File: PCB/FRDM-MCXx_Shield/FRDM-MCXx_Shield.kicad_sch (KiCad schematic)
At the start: 16 parts, among them J2 Conn_01x03_Pin, J3 Conn_01x02_Pin, J4 Conn_01x04_Pin, J5 Barrel_Jack_Switch, Q1 IRLML6401, U1 M95010-RMN6TP

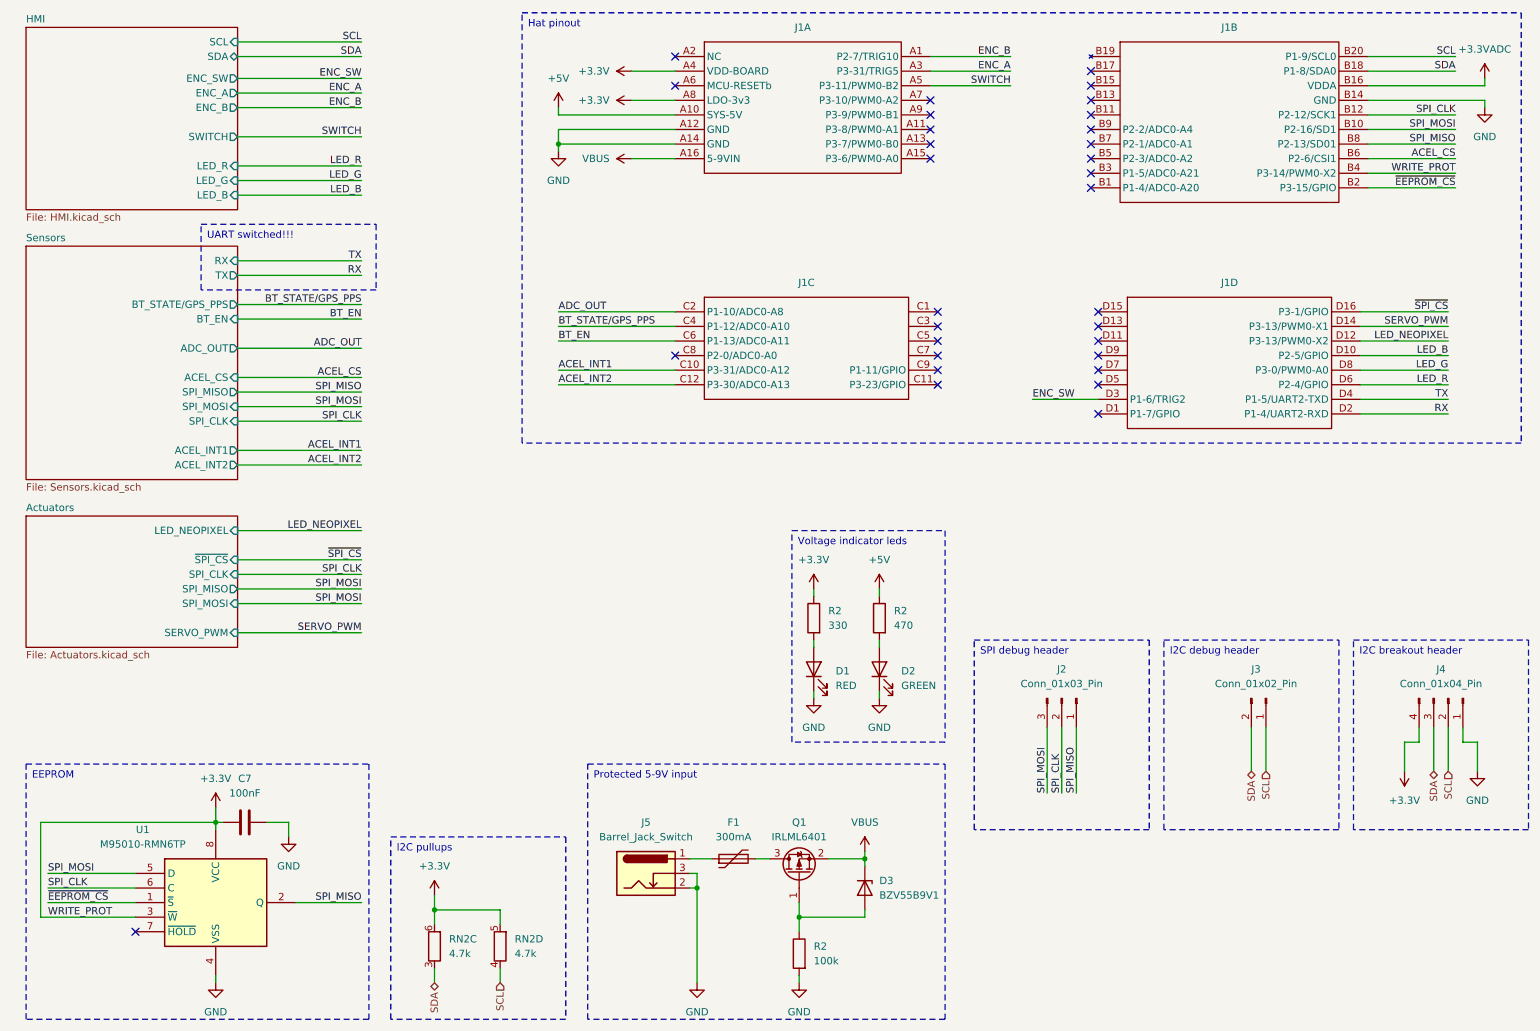
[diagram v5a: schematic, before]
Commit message: Update
Schematic: Fixed pinout, removed 5-9vin and a bunch of other stuff. Changed button/encoder debouncing.

PCB: Fixed pinout, layout and labeling. Added extra resisitors and capacitors.
Added diode direction markers.
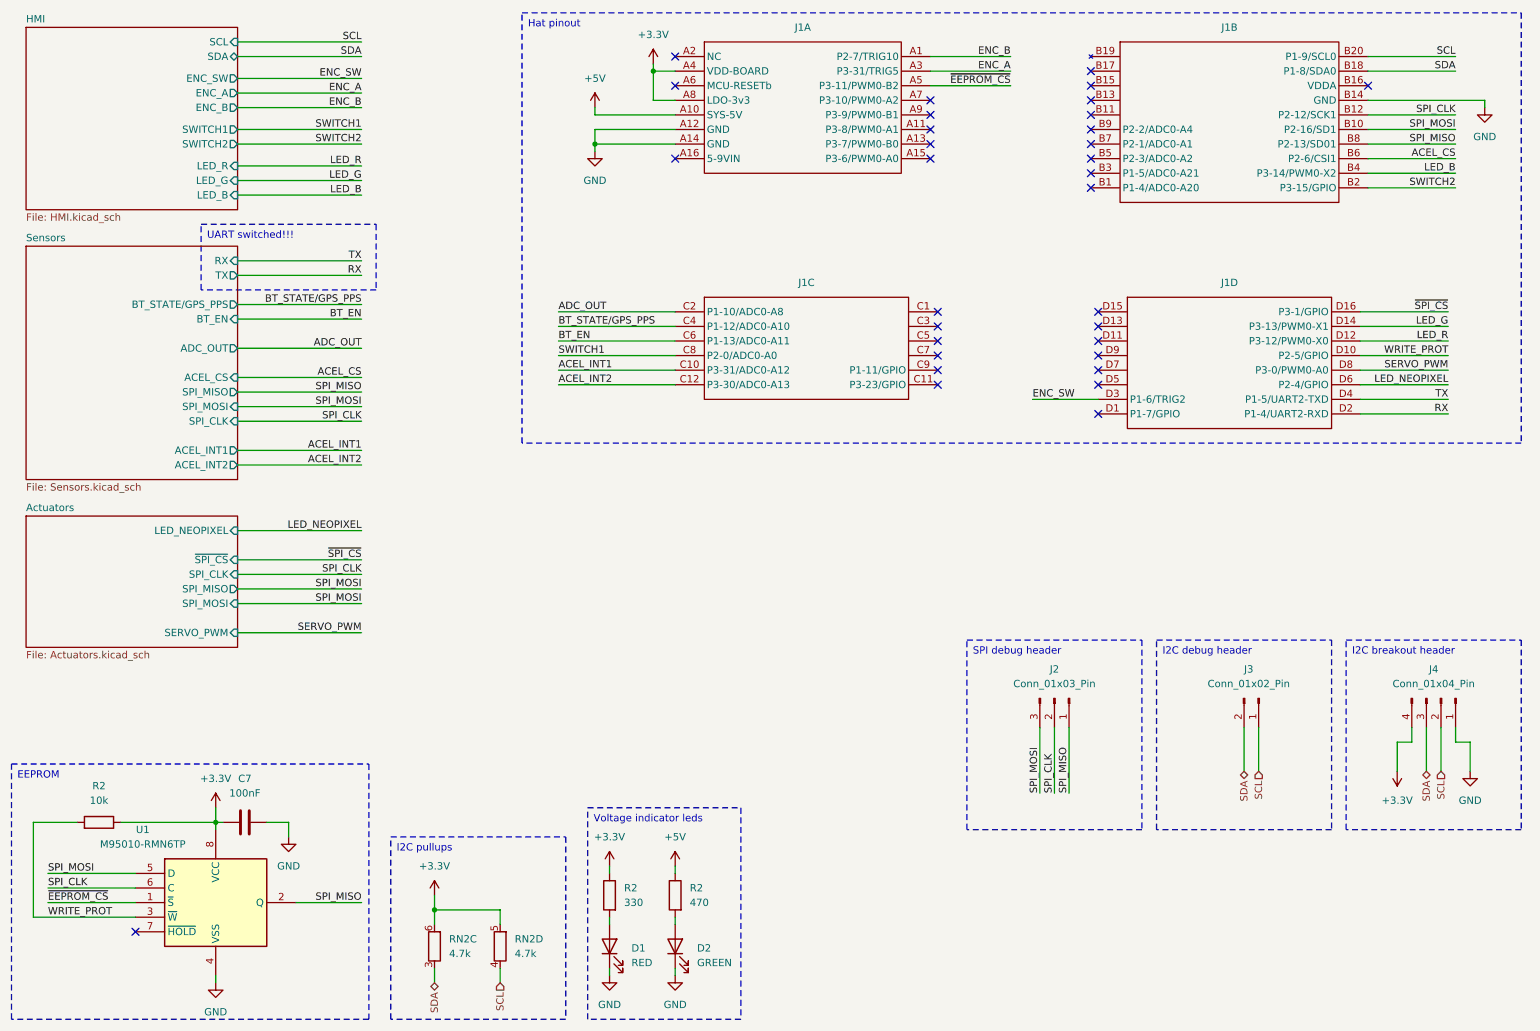
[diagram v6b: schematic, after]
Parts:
- removed D3: BZV55B9V1, Diode_SMD:D_SOD-128, symbol Diode:BZV55B9V1
- removed F1: 300mA, Fuse:Fuse_1206_3216Metric_Pad1.42x1.75mm_HandSolder, symbol Device:Polyfuse
- removed J5: Barrel_Jack_Switch, BarrelJack_Wuerth_6941xx301002, symbol Connector:Barrel_Jack_Switch
- removed Q1: IRLML6401, Package_TO_SOT_SMD:SOT-23, symbol Transistor_FET:IRLML6401
- J2: footprint Connector_PinHeader_2.54mm:PinHeader_1x03_P2.54mm_Vertical -> Connector_PinSocket_2.54mm:PinSocket_1x03_P2.54mm_Vertical
- J3: footprint Connector_PinHeader_2.54mm:PinHeader_1x02_P2.54mm_Vertical -> Connector_PinSocket_2.54mm:PinSocket_1x02_P2.54mm_Vertical
- J4: footprint Connector_PinHeader_2.54mm:PinHeader_1x04_P2.54mm_Vertical -> Connector_PinSocket_2.54mm:PinSocket_1x04_P2.54mm_Vertical
- R2: value 100k -> 10k
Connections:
- net SWITCH is gone; now on net ~{EEPROM_CS}: J1.A5 (P3-11/PWM0-B2)
- net +3.3V: now also R2.1; no longer J1.B4 (P3-14/PWM0-X2), U1.3 (~{W})
- net GND: no longer R2.2
- net LED_B: now also J1.B4 (P3-14/PWM0-X2); no longer J1.D10 (P2-5/GPIO)
- net LED_G: now also J1.D14 (P3-13/PWM0-X1); no longer J1.D8 (P3-0/PWM0-A0)
- net LED_NEOPIXEL: now also J1.D6 (P2-4/GPIO); no longer J1.D12 (P3-13/PWM0-X2)
- net LED_R: now also J1.D12 (P3-12/PWM0-X0); no longer J1.D6 (P2-4/GPIO)
- net SERVO_PWM: now also J1.D8 (P3-0/PWM0-A0); no longer J1.D14 (P3-13/PWM0-X1)
- net ~{EEPROM_CS}: no longer J1.B2 (P3-15/GPIO)
- net SWITCH1: now reaches J1.C8 (P2-0/ADC0-A0)
- net +3.3VADC: no longer names the net of J1.B16 (VDDA)
- net VBUS: no longer names the net of J1.A16 (5-9VIN)
- new net SWITCH2: J1.B2 (P3-15/GPIO)
- new net WRITE_PROT: J1.D10 (P2-5/GPIO), R2.2, U1.3 (~{W})
- no-connect marks 31 -> 32
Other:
- sheet HMI ports: added SWITCH1, SWITCH2; removed SWITCH
- moved on the sheet: D1, D2, J2, J3, J4, R2

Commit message: Updated footprint, PCB and schematic
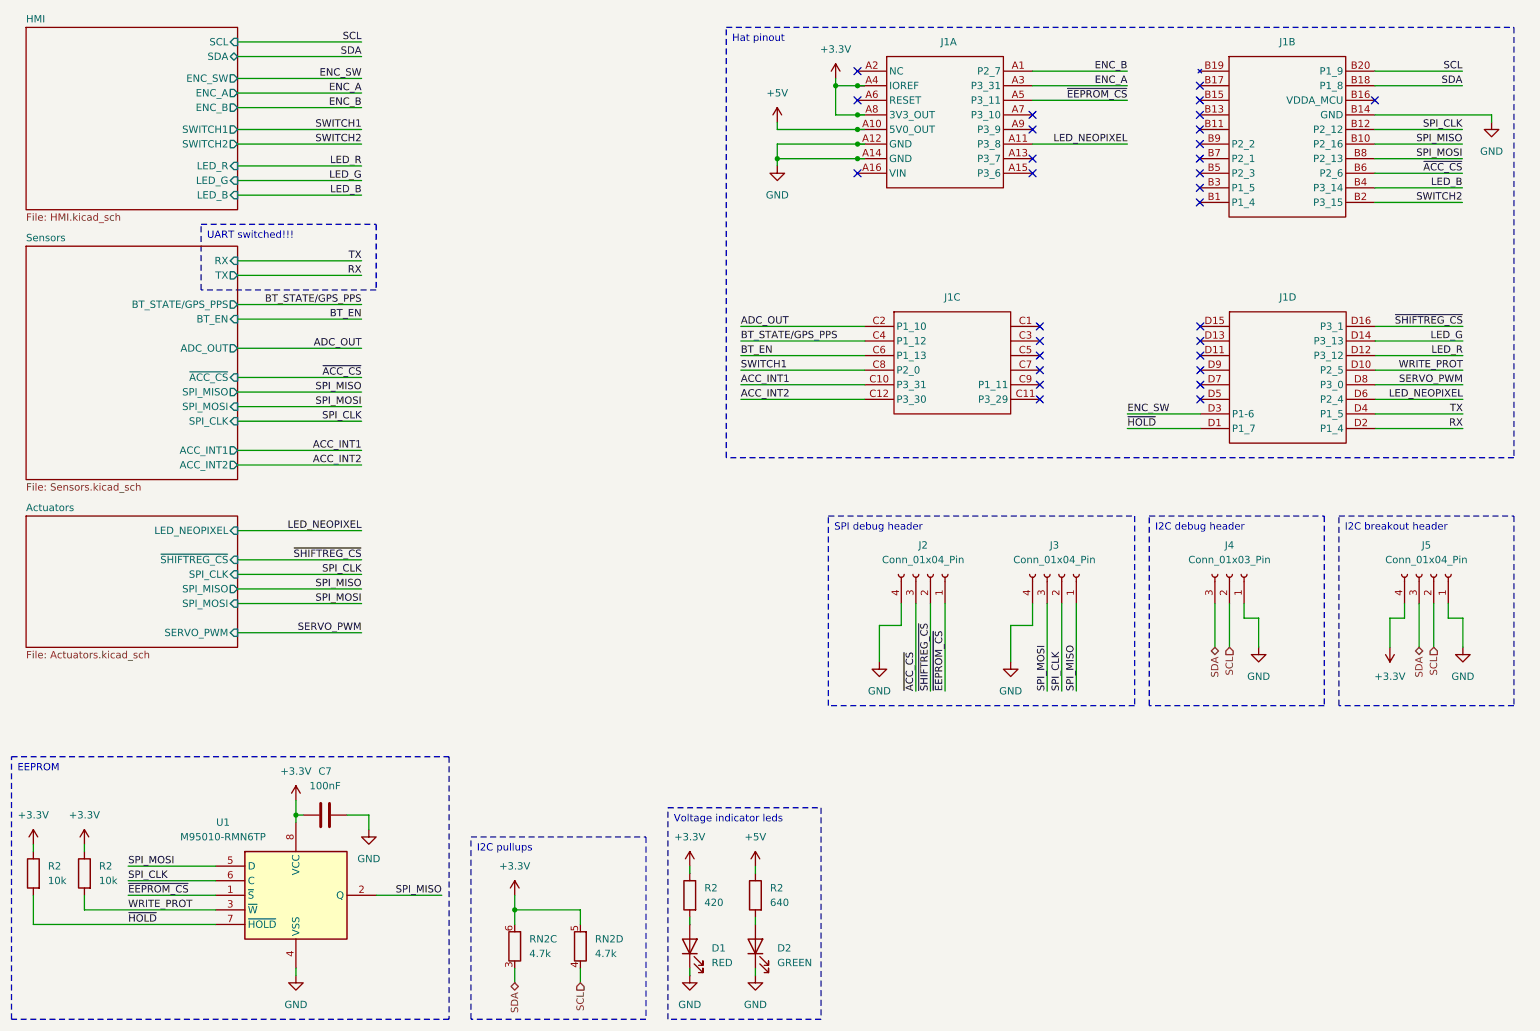
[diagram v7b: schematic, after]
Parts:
- removed J2: Conn_01x03_Pin, Connector_PinSocket_2.54mm:PinSocket_1x03_P2.54mm_Vertical, symbol Connector:Conn_01x03_Pin
- removed J3: Conn_01x02_Pin, Connector_PinSocket_2.54mm:PinSocket_1x02_P2.54mm_Vertical, symbol Connector:Conn_01x02_Pin
- removed J4: Conn_01x04_Pin, Connector_PinSocket_2.54mm:PinSocket_1x04_P2.54mm_Vertical, symbol Connector:Conn_01x04_Pin
- added J2, J3, J5: Conn_01x04_Pin, Connector_PinSocket_2.54mm:PinSocket_1x04_P2.54mm_Vertical, symbol Connector:Conn_01x04_Socket
- added J4: Conn_01x03_Pin, Connector_PinHeader_2.54mm:PinHeader_1x03_P2.54mm_Vertical, symbol Connector:Conn_01x03_Socket
- added R2: 10k, Resistor_SMD:R_0603_1608Metric_Pad0.98x0.95mm_HandSolder, symbol Device:R
- R2: value 470 -> 640
- R2: value 330 -> 420
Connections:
- net +3.3V: now also J5.4 (Pin_4), R2.1
- net GND: now also J2.4 (Pin_4), J3.4 (Pin_4), J4.1 (Pin_1), J5.1 (Pin_1)
- net LED_NEOPIXEL: now also J1.A11 (P3_8)
- net SCL: now also J4.2 (Pin_2), J5.2 (Pin_2)
- net SDA: now also J4.3 (Pin_3), J5.3 (Pin_3)
- net SPI_CLK: now also J3.2 (Pin_2)
- net SPI_MISO: now also J1.B10 (P2_16), J3.1 (Pin_1); no longer J1.B8 (P2-13/SD01)
- net SPI_MOSI: now also J1.B8 (P2_13), J3.3 (Pin_3); no longer J1.B10 (P2-16/SD1)
- net ~{EEPROM_CS}: now also J2.1 (Pin_1)
- net ~{HOLD}: now reaches J1.D1 (P1_7)
- net ~{HOLD}: now also U1.7 (~{HOLD}), R2.2
- net ACEL_CS renamed ~{ACC_CS}
- net ~{ACC_CS}: now also J2.3 (Pin_3)
- net ACEL_INT1 renamed ACC_INT1
- net ACEL_INT2 renamed ACC_INT2
- net ~{SPI_CS} renamed ~{SHIFTREG_CS}
- net ~{SHIFTREG_CS}: now also J2.2 (Pin_2)
- no-connect marks 32 -> 29
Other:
- sheet Actuators ports: added ~{SHIFTREG_CS}; removed ~{SPI_CS}
- sheet Sensors ports: added ACC_INT1, ACC_INT2, ~{ACC_CS}; removed ACEL_CS, ACEL_INT1, ACEL_INT2
- moved on the sheet: C7, D1, D2, J1A, J1B, J1C, J1D, R2, RN2C, RN2D, U1

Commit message: Updated PCB and added bill of materials
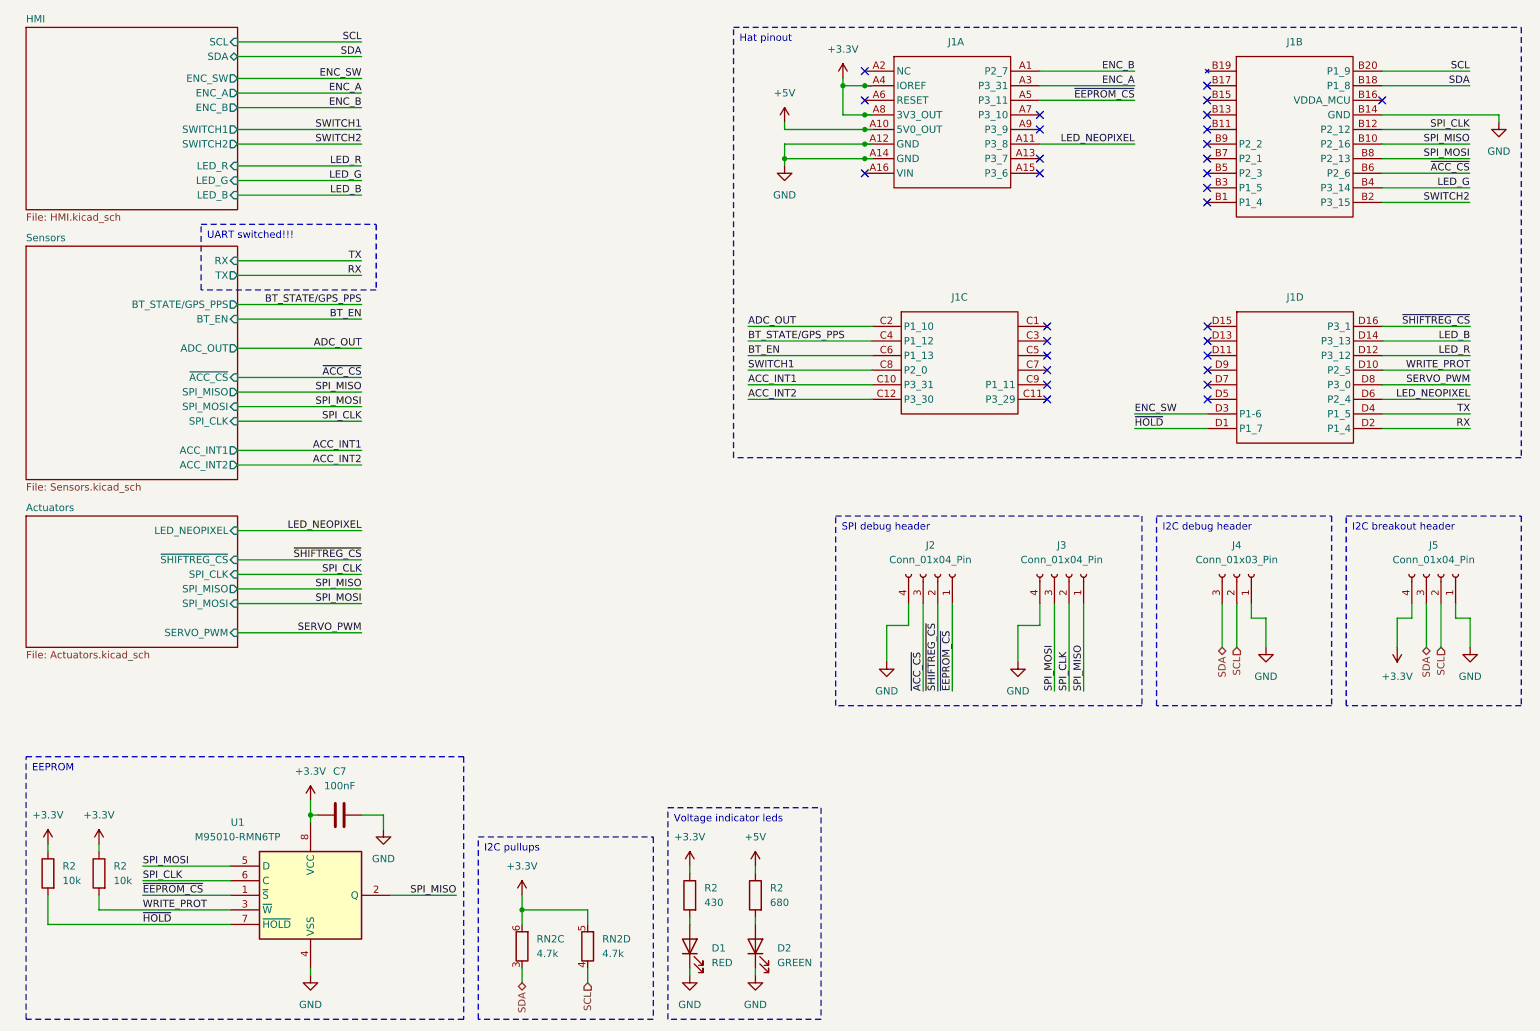
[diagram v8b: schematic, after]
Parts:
- C7: GPN (none) -> GPC0603104
- J2, J3, J5: GPN (none) -> GPHA-1X04
- J4: footprint Connector_PinHeader_2.54mm:PinHeader_1x03_P2.54mm_Vertical -> Connector_PinSocket_2.54mm:PinSocket_1x03_P2.54mm_Vertical; GPN (none) -> GPHA-1X03
- R2: GPN (none) -> GPR060310K
- R2: value 640 -> 680; GPN (none) -> GPR0603640R
- R2: value 420 -> 430; GPN (none) -> GPR0603420R
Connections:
- net LED_B: now also J1.D14 (P3_13); no longer J1.B4 (P3_14)
- net LED_G: now also J1.B4 (P3_14); no longer J1.D14 (P3_13)
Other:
- moved on the sheet: C7, J1A, J1B, J1C, J1D, J2, J3, J4, J5, R2, RN2C, RN2D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
